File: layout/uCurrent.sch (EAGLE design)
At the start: 26 parts, among them SW1 DP3T, SW2 DP3T, U1 MAX4239ASA, U2 LMV321M5X, U3 TPS3809L30DBVR

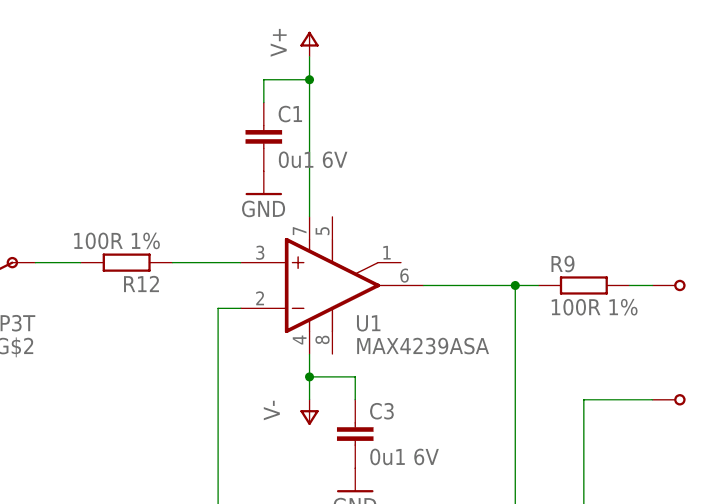
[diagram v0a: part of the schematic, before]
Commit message: Forgot first Pin on OpAmp
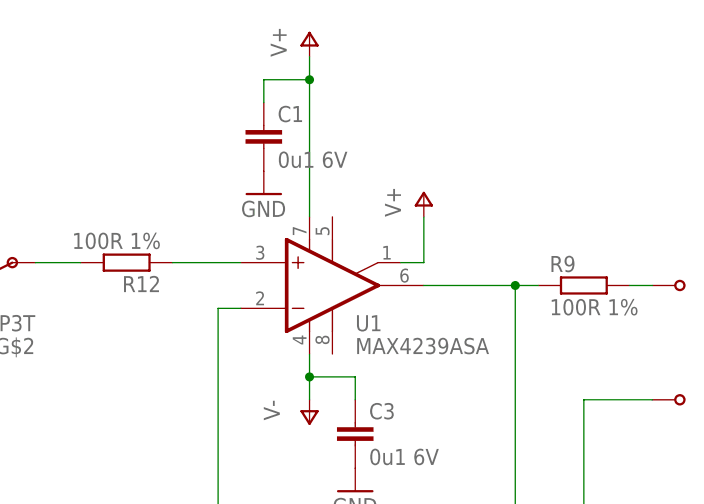
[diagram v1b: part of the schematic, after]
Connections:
- net V+: now also U1.NC
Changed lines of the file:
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@@
 <part name="C2" library="rcl" deviceset="C-EU" device="C0805" value="0u1 6V"/>
 <part name="C1" library="rcl" deviceset="C-EU" device="C0805" value="0u1 6V"/>
+<part name="P+1" library="supply1" deviceset="V+" device=""/>
 </parts>
 <sheets>
@@
 <instance part="C2" gate="G$1" x="144.78" y="43.18"/>
 <instance part="C1" gate="G$1" x="182.88" y="119.38"/>
+<instance part="P+1" gate="1" x="200.66" y="111.76"/>
 </instances>
 <busses>
@@
 <pinref part="C2" gate="G$1" pin="1"/>
 </segment>
+<segment>
+<pinref part="U1" gate="G$1" pin="NC"/>
+<pinref part="P+1" gate="1" pin="V+"/>
+<wire x1="198.12" y1="104.14" x2="200.66" y2="104.14" width="0.1524" layer="91"/>
+<wire x1="200.66" y1="104.14" x2="200.66" y2="109.22" width="0.1524" layer="91"/>
+</segment>
 </net>
